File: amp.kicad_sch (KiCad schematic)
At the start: 44 parts, among them J1 Conn_Coaxial, Q1 J111, Q2 MMBF4393, U1 AD8933_module, U10 TL072, U11 LM7171, U3 AD8039, U4 TL072, U5 AD5258BRM, U6 AD8039, U7 LM393LVDDFR, U8 FSA3157L6X, U9 FSA3157L6X

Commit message: Savegame.
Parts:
- removed C1, C2: 100n, Capacitor_SMD:C_0603_1608Metric_Pad1.08x0.95mm_HandSolder, symbol Device:C
- added C25, C34, C35, C51, C53, C57, C58, C61, C62, C63, C64, C65, C66, C67, C68: 100n, Capacitor_SMD:C_0603_1608Metric_Pad1.08x0.95mm_HandSolder, symbol Device:C
- added C26, C27, C28, C33: 1u, Resistor_SMD:R_0603_1608Metric_Pad0.98x0.95mm_HandSolder, symbol Device:C
- added C29, C30, C59, C60: 100n, Resistor_SMD:R_0603_1608Metric_Pad0.98x0.95mm_HandSolder, symbol Device:C
- added C31, C32: 1n, Resistor_SMD:R_0603_1608Metric_Pad0.98x0.95mm_HandSolder, symbol Device:C
- added C38, C39, C40: 22p, Capacitor_SMD:C_0603_1608Metric_Pad1.08x0.95mm_HandSolder, symbol Device:C
- added C41: 33p, Capacitor_SMD:C_0603_1608Metric_Pad1.08x0.95mm_HandSolder, symbol Device:C
- added C42: 1p, Capacitor_SMD:C_0603_1608Metric_Pad1.08x0.95mm_HandSolder, symbol Device:C
- added C43: 5.6p, Capacitor_SMD:C_0603_1608Metric_Pad1.08x0.95mm_HandSolder, symbol Device:C
- added C44: 4.7p, Capacitor_SMD:C_0603_1608Metric_Pad1.08x0.95mm_HandSolder, symbol Device:C
- added C52, C54: 2.2u, Capacitor_SMD:C_1206_3216Metric_Pad1.33x1.80mm_HandSolder, symbol Device:C
- added C55, C56: 10n, Capacitor_SMD:C_0603_1608Metric_Pad1.08x0.95mm_HandSolder, symbol Device:C
- added FB1, FB2: FerriteBead, Inductor_SMD:L_0603_1608Metric_Pad1.05x0.95mm_HandSolder, symbol Device:FerriteBead
- added J4, J6: Conn_01x03_Pin, Connector_PinHeader_2.54mm:PinHeader_1x03_P2.54mm_Vertical, symbol Connector:Conn_01x03_Pin
- added L3: 470n, Inductor_SMD:L_0603_1608Metric, symbol Device:L
- added L4, L5: 390n, Inductor_SMD:L_0603_1608Metric, symbol Device:L
- added R23: 100k, Resistor_SMD:R_0603_1608Metric_Pad0.98x0.95mm_HandSolder, symbol Device:R_US
- added R24, R49, R50: 1k, Resistor_SMD:R_0603_1608Metric_Pad0.98x0.95mm_HandSolder, symbol Device:R_US
- added R48: 50, Resistor_SMD:R_0603_1608Metric_Pad0.98x0.95mm_HandSolder, symbol Device:R_US
- added unit 2 of U8
- added unit 2 of U9
- C3: footprint (none) -> Resistor_SMD:R_0603_1608Metric_Pad0.98x0.95mm_HandSolder
- C6: value 1u -> 100n; footprint (none) -> Capacitor_SMD:C_0603_1608Metric_Pad1.08x0.95mm_HandSolder
- Q1: footprint Package_TO_SOT_THT:TO-92 -> Package_TO_SOT_THT:TO-92_Inline_Wide
- R17: value 1k -> 100k
- U10, U4: footprint (none) -> Package_SO:SOIC-8_3.9x4.9mm_P1.27mm
- U8, U9: footprint Package_TO_SOT_SMD:SOT-363_SC-70-6 -> Package_TO_SOT_SMD:SOT-23-6_Handsoldering
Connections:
- net +3V3 is gone; now on net +5V: C5.1
- net +16.5V: now also C51.1, C52.1, C55.1, C61.1, C63.1
- net +5V: now also C3.2, U5.8 (VDD), U7.5 (+), C27.2, C29.2, C31.2, C59.2, C65.1, C66.1, U8.5 (V+), U9.5 (V+); no longer C4.1, R13.2, U1.1 (V_{cc})
- net -16.5V: now also C53.1, C54.1, C56.1, C62.1, C64.1
- net -5V: now also C26.2, C28.2, C30.2, C32.2, C60.2
- net GND: now also C3.1, U7.6 (-), C25.2, C26.1, C27.1, C28.1, C29.1, C30.1, C31.1, C32.1, C33.1, C34.2, C35.2, C38.2, C39.2, C40.2, C41.2, C51.2, C52.2, C53.2, C54.2, C55.2, C56.2, C57.2, C58.2, C59.1, C60.1, C61.2, C62.2, C63.2, C64.2, C65.2, C66.2, C67.2, C68.2, J4.3 (Pin_3), J6.3 (Pin_3), U8.2 (GND), U9.2 (GND); no longer C3.2
- net OUT_3V3: now also U3.6 (-), U3.7; no longer U3.1, U3.2 (-)
- net PWM_THRS_DAC: now also R49.1; no longer U7.3 (+)
- net at U3.3 (+): now also U9.3, C40.1, C44.2, L5.2; no longer U9.4
- net at C6.1, R17.2: now also R23.1; no longer U10.3 (+)
- net at R2.2, R6.1: now also U3.2 (-); no longer U6.2 (-)
- net at Q1.1 (D), Q2.1 (D), R11.2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: now also U6.3 (+); no longer U3.5 (+)
- net SDATA_SG: now reaches U1.3 (SDATA)
- net SCK_SG: now reaches U1.4 (SCLK)
- net FSYNC_SG: now reaches U1.5 (FSYNC)
- net at U10.5 (+): now also C68.1, R50.2
- net at U10.6 (-): now also U10.7, U7.3 (+)
- net at R8.2, U7.2 (-), U8.3: now also U3.1; no longer U6.1
- net at R27.2, R28.1, U11.6: now also R48.2
- net at U5.2 (AD0): now also J6.2 (Pin_2)
- net at U5.3 (AD1): now also J4.2 (Pin_2)
- net SDA_2: now reaches U5.4 (SDA)
- net SCL_2: now reaches U5.5 (SCL)
- net +3.3V: now reaches U5.6 (V_{LOGIC})
- net +3.3V: now also C35.1, FB1.1, FB2.2, J4.1 (Pin_1), J6.1 (Pin_1)
- net at J1.1 (In), R28.2: now also R48.1
- new net: C57.1, R1.2, R24.1
- new net: U3.5 (+), U9.4
- new net: C33.2, C4.1, FB1.2, U1.1 (V_{cc})
- new net: C34.1, FB2.1, R13.2
- new net: C58.1, R24.2, U4.3 (+)
- new net: C38.1, C42.1, L3.1, U1.7 (OUT)
- new net: C25.1, R23.2, U10.3 (+)
- new net: C67.1, R49.2, R50.1
- new net: C41.1, C42.2, C43.1, L3.2, L4.1
- new net: C39.1, C43.2, C44.1, L4.2, L5.1
- new net: R15.1, U6.1, U6.2 (-)
- no-connect marks 0 -> 1
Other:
- moved on the sheet: C4, C5, C6, R1, R13, R15, R16, R17, R2, R6, R8, U10B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

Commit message: Add the tested push-pull rail generator.
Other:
- note added: "MORA DA IZDRŽI NEKOLIKO WATI"
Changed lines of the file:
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@@
+		)
+	)
+	(text "MORA DA IZDRŽI NEKOLIKO WATI"
+		(exclude_from_sim no)
+		(at 367.538 180.848 0)
+		(effects
+			(font
+				(size 1.27 1.27)
+			)
 		)
 	)

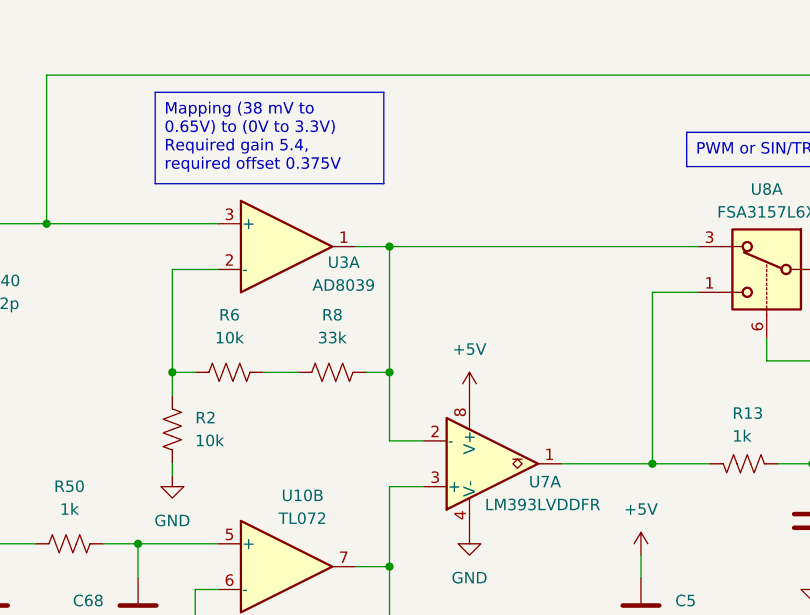
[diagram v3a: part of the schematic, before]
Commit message: SEPIC and CUK
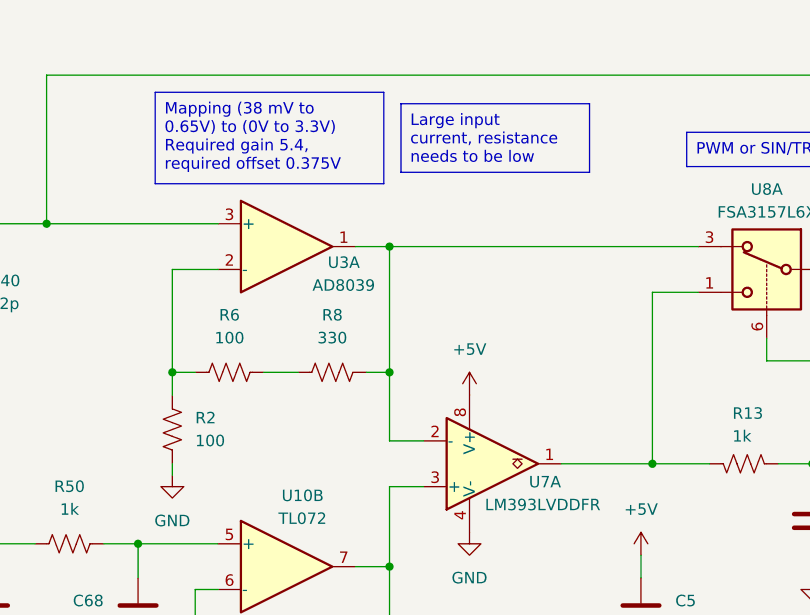
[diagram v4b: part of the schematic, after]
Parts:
- R2, R6: value 10k -> 100
- R8: value 33k -> 330
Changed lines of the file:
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@@
 		)
 	)
+	(text_box "Large input current, resistance needs to be low\n"
+		(exclude_from_sim no)
+		(at 207.01 34.925 0)
+		(size 20.955 7.62)
+		(stroke
+			(width 0)
+			(type default)
+		)
+		(fill
+			(type color)
+			(color 63 170 255 1)
+		)
+		(effects
+			(font
+				(size 1.27 1.27)
+				(color 255 0 0 1)
+			)
+			(justify left top)
+		)
+	)
 	(text_box "3x gain,\nmapping for 20 Vpp"
 		(exclude_from_sim no)
@@
 			)
 		)
-		(property "Value" "10k"
+		(property "Value" "100"
 			(at 184.15 72.3899 0)
 			(effects
@@
 			)
 		)
-		(property "Value" "10k"
+		(property "Value" "100"
 			(at 187.96 60.96 90)
 			(effects
@@
 			)
 		)
-		(property "Value" "33k"
+		(property "Value" "330"
 			(at 199.39 60.96 90)
 			(effects

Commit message: .
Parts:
- R15, R20, R26: value 1k -> 100
- R16, R25: value 2.2k -> 200
- R27: value 2k -> 200
- R28, R48: value 50 -> 100
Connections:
- net +16.5V: no longer U10.8 (V+), U11.7 (V+)
- net -16.5V: no longer U10.4 (V-), U11.4 (V-)
- new net +15.3V: U10.8 (V+), U11.7 (V+)
- new net -15.3V: U10.4 (V-), U11.4 (V-)
